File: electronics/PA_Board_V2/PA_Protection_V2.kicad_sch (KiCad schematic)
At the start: 61 parts, among them J10 Conn_01x05, J2 Conn_01x04, J3 Conn_01x05, J6 Conn_01x06, J9 USB_B_Micro, SW1 SW_Push, U12 LM2904, U13 ATSAMD21E18A-A, U15 74LV1T34, U2 LM75B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

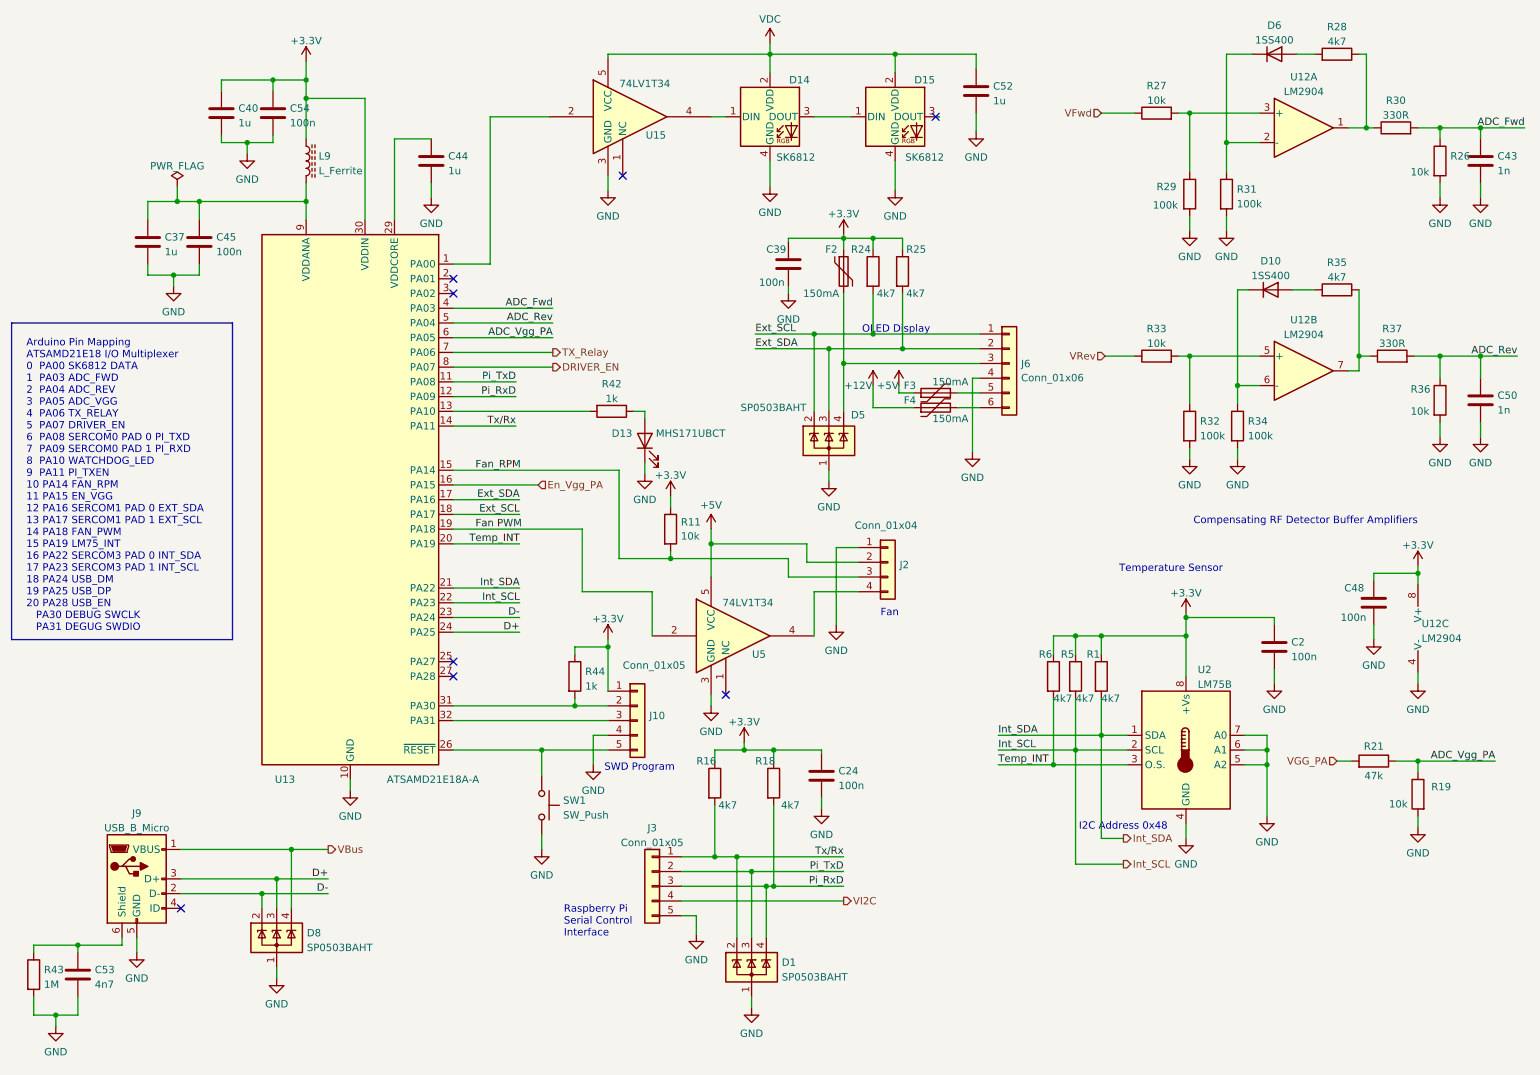
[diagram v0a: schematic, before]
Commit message: Update Arduino documentation and change to Kicad V8
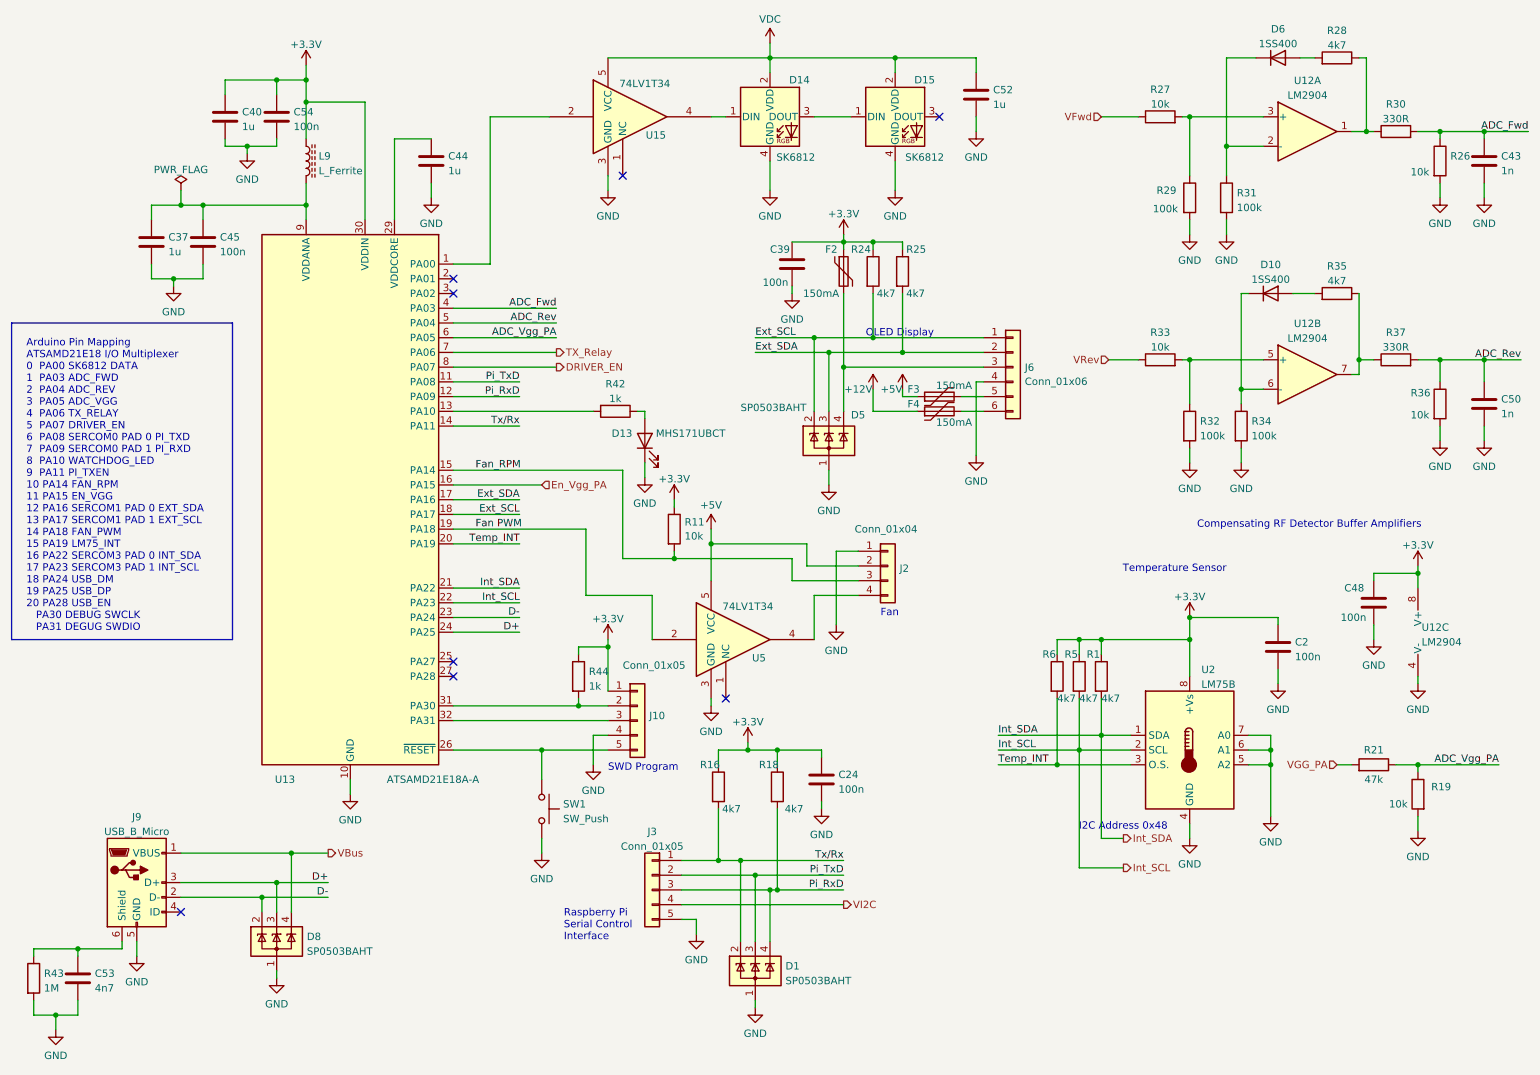
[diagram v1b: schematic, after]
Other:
- moved on the sheet: C2, C24, C37, C39, C40, C43, C45, C50, C52, C53, C54, D1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

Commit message: Updates in electronics bits and bobs
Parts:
- added F5, F6: 150mA, Fuse:Fuse_0805_2012Metric, symbol Device:Polyfuse
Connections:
- net +12V: now also F5.1
- net +5V: now also F6.1; no longer J2.2 (Pin_2)
- new net: F5.2, F6.2, J2.2 (Pin_2)
